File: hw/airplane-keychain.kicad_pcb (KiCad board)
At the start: 2 copper layers, 101.8 x 122.1 mm, 21 parts, among them IC1 ATTINY85-P, SW1 SW_PUSH, SW2 SPST

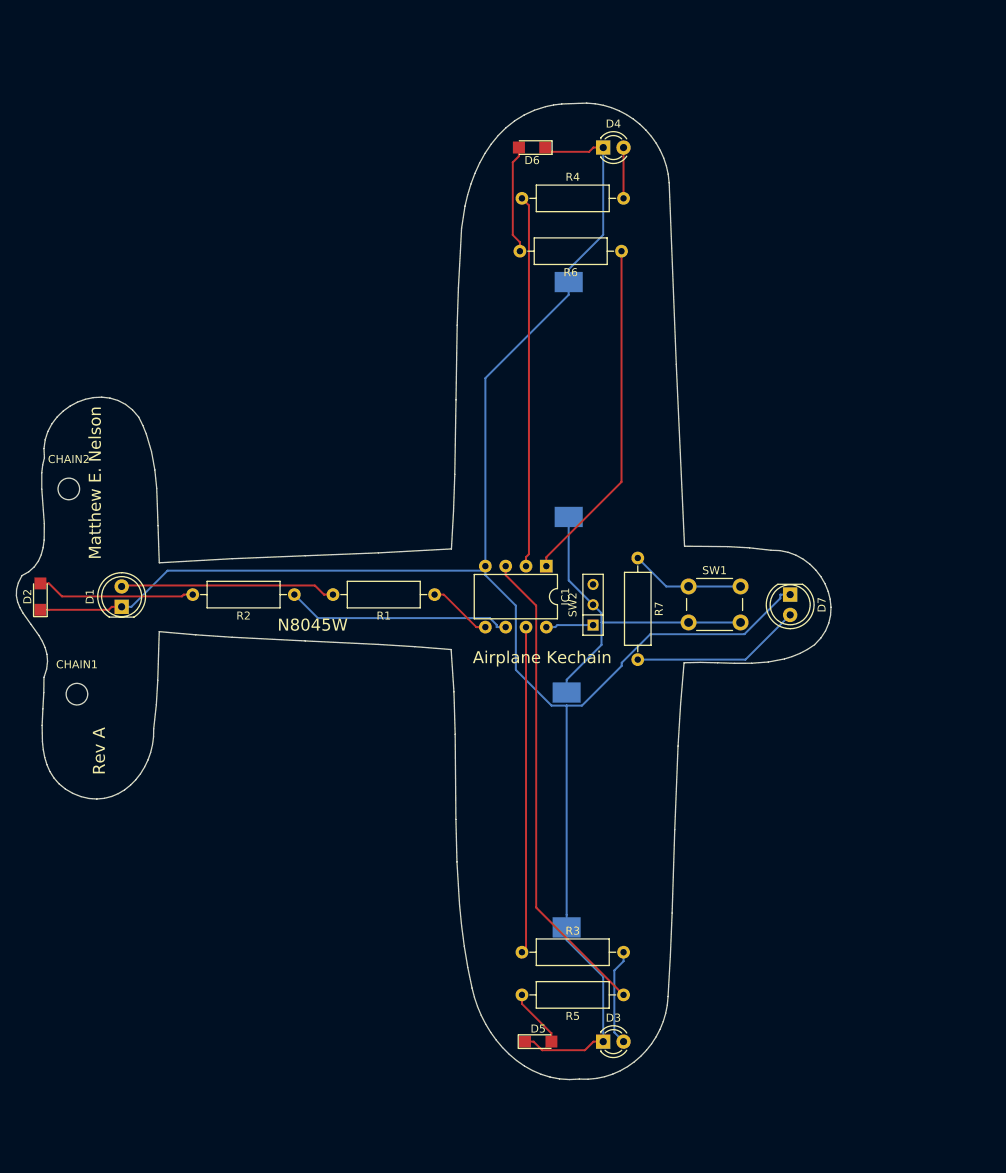
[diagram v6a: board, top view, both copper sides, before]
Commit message: Switch to new PCB cutout
Switch to new PCB cutout.  Added files for generating boards using
OpenSCAD.  Cleaned up some files.
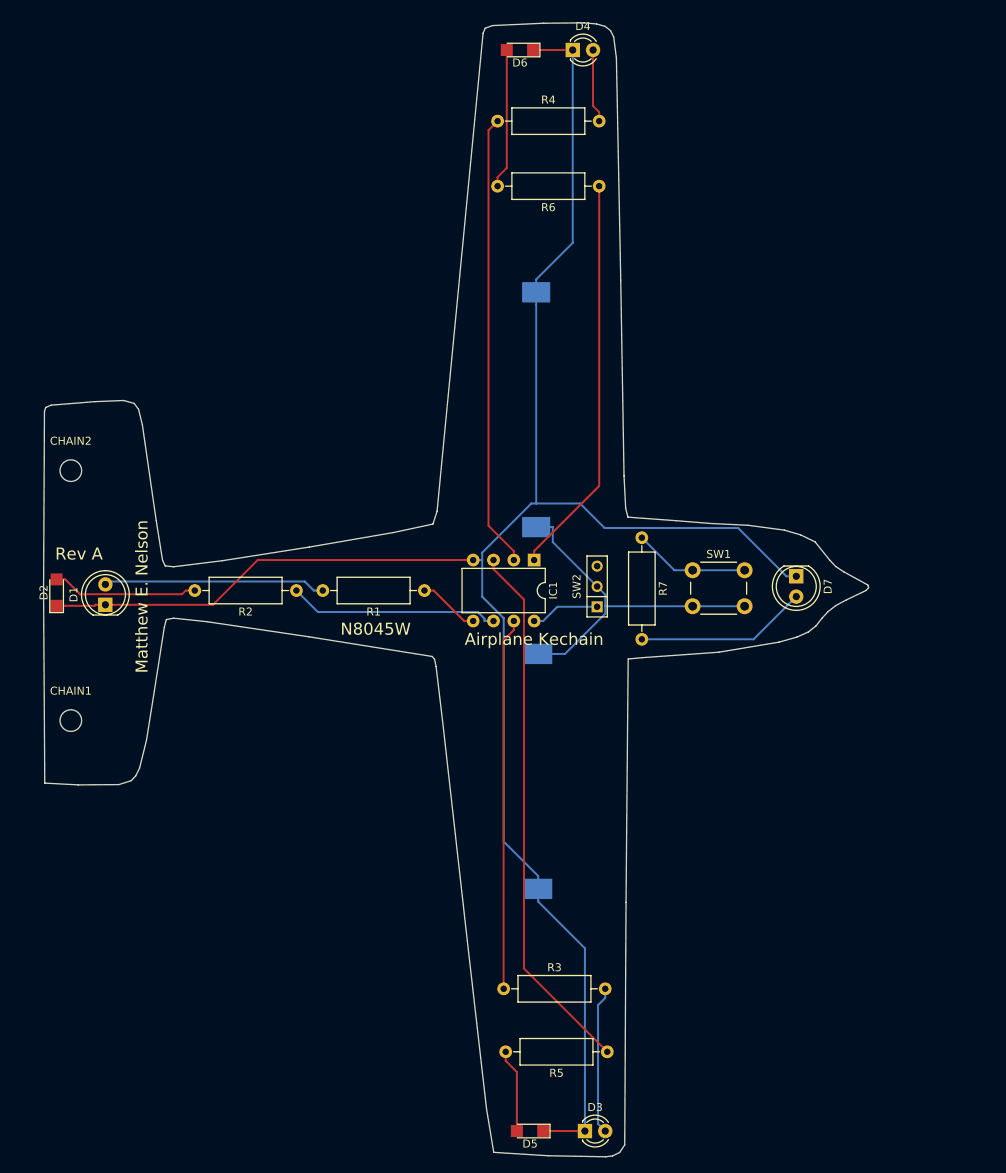
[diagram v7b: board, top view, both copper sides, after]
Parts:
- moved D4 12.8 mm to (147.3, 28.2)
- moved D6 12.3 mm to (140.7, 28.2)
- moved D3 11.4 mm to (148.8, 163.3)
- moved D5 11.2 mm to (142.0, 163.3), turned to 180 degrees
- moved R4 10.1 mm to (137.9, 37.1)
- moved R6 8.59 mm to (150.6, 45.2)
- moved R5 7.40 mm to (151.6, 153.4)
- moved BT2 5.99 mm to (143.0, 118.4)
- moved R3 5.11 mm to (138.7, 145.5)
- moved BT1 4.26 mm to (142.7, 73.2)
- moved CHAIN1 3.39 mm to (84.6, 112.0)
- moved R7 2.59 mm to (156.0, 89.2)
- moved D7 2.41 mm to (175.3, 94.0)
- moved SW2 2.34 mm to (150.4, 95.2)
- moved CHAIN2 2.30 mm to (84.6, 80.8)
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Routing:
- net GND: track 235.6 -> 247.5 mm
- net Net-(IC1-Pad2): track 46.5 -> 56.6 mm
- net Net-(IC1-Pad3): track 59.7 -> 67.4 mm
- net Net-(IC1-Pad1): track 43.3 -> 50.1 mm
- net Net-(D3-Pad2): track 12.1 -> 18.5 mm
- net Net-(IC1-Pad7): track 40.9 -> 46.5 mm
- net Net-(D6-Pad2): track 13.6 -> 17.5 mm
- net Net-(D5-Pad2): track 7.39 -> 10.5 mm
- net Net-(D4-Pad2): track 6.35 -> 9.21 mm
- net Net-(IC1-Pad8): track 5.95 -> 8.61 mm
- net Net-(IC1-Pad6): track 28.3 -> 26.4 mm
- net Net-(D2-Pad2): track 19.8 -> 18.2 mm
- net Net-(D1-Pad2): track 26.9 -> 27.8 mm
- net Net-(BT1-Pad1): track 42.8 -> 43.5 mm
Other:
- board size 101.8 x 122.1 mm -> 103.1 x 141.7 mm
